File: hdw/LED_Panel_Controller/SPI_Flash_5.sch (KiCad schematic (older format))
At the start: 14 parts, among them U2901 74LVC1G97, U2902 SST25VF080B-50-4I-S2AF

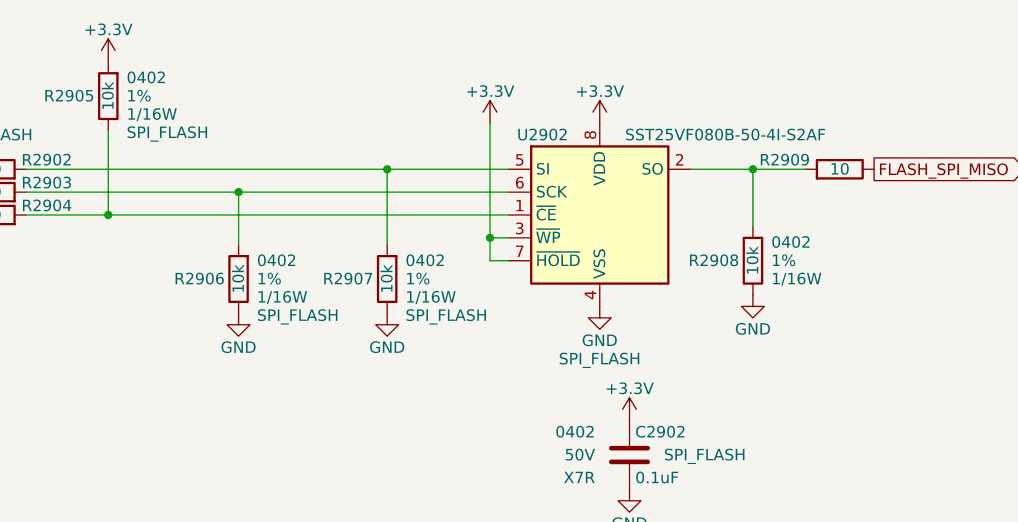
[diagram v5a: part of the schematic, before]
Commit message: fixed SPI flash pull resistors, more PCB placement
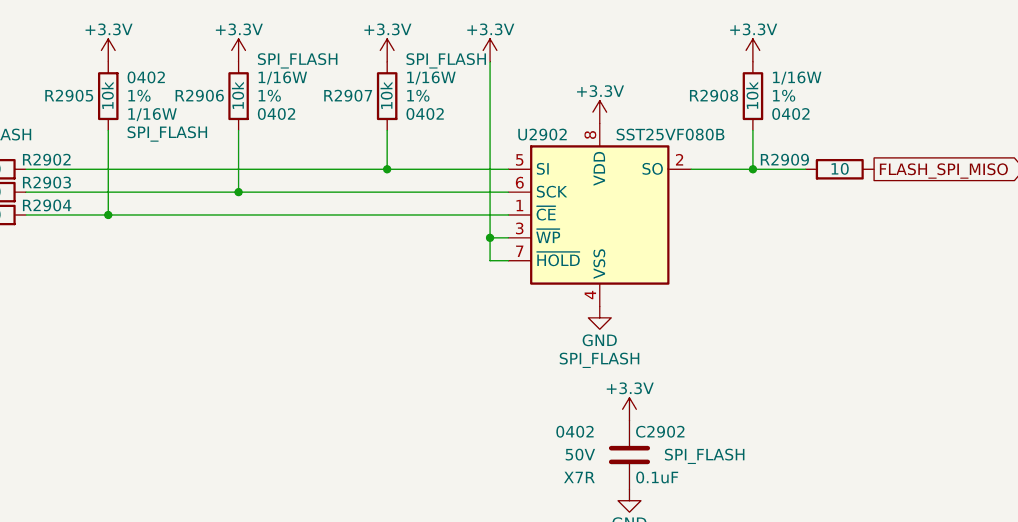
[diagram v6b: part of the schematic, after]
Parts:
- U2902: value SST25VF080B-50-4I-S2AF -> SST25VF080B
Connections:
- net +3V3: now also R2906.2, R2907.2, R2908.2
- net GND: no longer R2906.2, R2907.2, R2908.2
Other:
- moved on the sheet: R2906, R2907, R2908
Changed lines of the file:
@@
 L Custom_Library:R_Custom R2908
 U 1 1 60786266
-P 6750 3850
-F 0 "R2908" H 6690 3850 50  0000 R CNN
-F 1 "10k" V 6750 3850 50  0000 C CNN
-F 2 "Resistors_SMD:R_0402" H 6750 3850 50  0001 C CNN
-F 3 "" H 6750 3850 50  0001 C CNN
-F 4 "0402" H 6830 3930 50  0000 L CNN "display_footprint"
-F 5 "1%" H 6830 3850 50  0000 L CNN "Tolerance"
-F 6 "1/16W" H 6830 3770 50  0000 L CNN "Wattage"
-F 7 "RMCF0402FT10K0CT-ND" H 7050 4250 60  0001 C CNN "Digi-Key PN"
-	1    6750 3850
-	1    0    0    -1
-$EndComp
-$Comp
-L power:GND #PWR02908
-U 1 1 60786271
-P 5150 4080
-F 0 "#PWR02908" H 5150 3830 50  0001 C CNN
-F 1 "GND" H 5150 3930 50  0000 C CNN
-F 2 "" H 5150 4080 50  0001 C CNN
-F 3 "" H 5150 4080 50  0001 C CNN
-	1    5150 4080
-	1    0    0    -1
-$EndComp
-$Comp
-L power:GND #PWR02914
-U 1 1 60786276
-P 6750 4000
-F 0 "#PWR02914" H 6750 3750 50  0001 C CNN
-F 1 "GND" H 6750 3850 50  0000 C CNN
-F 2 "" H 6750 4000 50  0001 C CNN
-F 3 "" H 6750 4000 50  0001 C CNN
-	1    6750 4000
-	1    0    0    -1
+P 6750 3130
+F 0 "R2908" H 6690 3130 50  0000 R CNN
+F 1 "10k" V 6750 3130 50  0000 C CNN
+F 2 "Resistors_SMD:R_0402" H 6750 3130 50  0001 C CNN
+F 3 "" H 6750 3130 50  0001 C CNN
+F 4 "0402" H 6830 3210 50  0000 L CNN "display_footprint"
+F 5 "1%" H 6830 3130 50  0000 L CNN "Tolerance"
+F 6 "1/16W" H 6830 3050 50  0000 L CNN "Wattage"
+F 7 "RMCF0402FT10K0CT-ND" H 7050 3530 60  0001 C CNN "Digi-Key PN"
+	1    6750 3130
+	1    0    0    1
 $EndComp
 $Comp
@@
 $EndComp
 Wire Wire Line
-	5150 3450 5150 3780
-Connection ~ 5150 3450
-Wire Wire Line
-	5150 3450 5680 3450
-Wire Wire Line
 	3930 3280 3930 3650
 Wire Wire Line
 	3930 3650 5680 3650
 Connection ~ 3930 3650
-Wire Wire Line
-	6980 3450 6750 3450
-Wire Wire Line
-	6750 3700 6750 3450
-Connection ~ 6750 3450
-Wire Wire Line
-	6750 3450 6480 3450
 Text GLabel 7280 3450 2    50   Output ~ 0
 FLASH_SPI_MISO
@@
 P 6080 3650
 F 0 "U2902" H 5830 4000 50  0000 C CNN
-F 1 "SST25VF080B-50-4I-S2AF" H 6630 4000 50  0000 C CNN
+F 1 "SST25VF080B" H 6630 4000 50  0000 R CNN
 F 2 "Package_SO:SOIC-8_5.275x5.275mm_P1.27mm" H 6080 2950 50  0001 C CNN
 F 3 "http://ww1.microchip.com/downloads/en/DeviceDoc/20005045C.pdf" H 6030 4200 50  0001 C CNN
@@
 L power:+3.3V #PWR02909
 U 1 1 5F69329F
-P 5600 3250
-F 0 "#PWR02909" H 5600 3100 50  0001 C CNN
-F 1 "+3.3V" H 5600 3390 50  0000 C CNN
-F 2 "" H 5600 3250 50  0001 C CNN
-F 3 "" H 5600 3250 50  0001 C CNN
-	1    5600 3250
+P 5600 2980
+F 0 "#PWR02909" H 5600 2830 50  0001 C CNN
+F 1 "+3.3V" H 5600 3120 50  0000 C CNN
+F 2 "" H 5600 2980 50  0001 C CNN
+F 3 "" H 5600 2980 50  0001 C CNN
+	1    5600 2980
 	1    0    0    -1
 $EndComp
@@
 	5680 3750 5600 3750
 Wire Wire Line
-	5600 3750 5600 3250
+	5600 3750 5600 2980
 Wire Wire Line
 	5680 3850 5600 3850
@@
 	5600 3850 5600 3750
 Connection ~ 5600 3750
-Wire Wire Line
-	3570 3550 4500 3550
 $Comp
 L Custom_Library:R_Custom R2906
 U 1 1 60786316
-P 4500 3930
-F 0 "R2906" H 4440 3930 50  0000 R CNN
-F 1 "10k" V 4500 3930 50  0000 C CNN
-F 2 "Resistors_SMD:R_0402" H 4500 3930 50  0001 C CNN
-F 3 "" H 4500 3930 50  0001 C CNN
-F 4 "0402" H 4580 4010 50  0000 L CNN "display_footprint"
-F 5 "1%" H 4580 3930 50  0000 L CNN "Tolerance"
-F 6 "1/16W" H 4580 3850 50  0000 L CNN "Wattage"
-F 7 "RMCF0402FT10K0CT-ND" H 4800 4330 60  0001 C CNN "Digi-Key PN"
-F 8 "SPI_FLASH" H 4580 3770 50  0000 L CNN "Configuration"
-	1    4500 3930
-	1    0    0    -1
-$EndComp
-$Comp
-L power:GND #PWR02907
-U 1 1 5F697052
-P 4500 4080
-F 0 "#PWR02907" H 4500 3830 50  0001 C CNN
-F 1 "GND" H 4500 3930 50  0000 C CNN
-F 2 "" H 4500 4080 50  0001 C CNN
-F 3 "" H 4500 4080 50  0001 C CNN
-	1    4500 4080
-	1    0    0    -1
-$EndComp
-Wire Wire Line
-	3570 3450 5150 3450
-Wire Wire Line
-	4500 3550 4500 3780
-Connection ~ 4500 3550
-Wire Wire Line
-	4500 3550 5680 3550
+P 4500 3130
+F 0 "R2906" H 4440 3130 50  0000 R CNN
+F 1 "10k" V 4500 3130 50  0000 C CNN
+F 2 "Resistors_SMD:R_0402" H 4500 3130 50  0001 C CNN
+F 3 "" H 4500 3130 50  0001 C CNN
+F 4 "0402" H 4580 3210 50  0000 L CNN "display_footprint"
+F 5 "1%" H 4580 3130 50  0000 L CNN "Tolerance"
+F 6 "1/16W" H 4580 3050 50  0000 L CNN "Wattage"
+F 7 "RMCF0402FT10K0CT-ND" H 4800 3530 60  0001 C CNN "Digi-Key PN"
+F 8 "SPI_FLASH" H 4580 2970 50  0000 L CNN "Configuration"
+	1    4500 3130
+	1    0    0    1
+$EndComp
 $Comp
 L Custom_Library:R_Custom R2903
@@
 L Custom_Library:R_Custom R2907
 U 1 1 60786356
-P 5150 3930
-F 0 "R2907" H 5090 3930 50  0000 R CNN
-F 1 "10k" V 5150 3930 50  0000 C CNN
-F 2 "Resistors_SMD:R_0402" H 5150 3930 50  0001 C CNN
-F 3 "" H 5150 3930 50  0001 C CNN
-F 4 "0402" H 5230 4010 50  0000 L CNN "display_footprint"
-F 5 "1%" H 5230 3930 50  0000 L CNN "Tolerance"
-F 6 "1/16W" H 5230 3850 50  0000 L CNN "Wattage"
-F 7 "RMCF0402FT10K0CT-ND" H 5450 4330 60  0001 C CNN "Digi-Key PN"
-F 8 "SPI_FLASH" H 5230 3770 50  0000 L CNN "Configuration"
-	1    5150 3930
-	1    0    0    -1
+P 5150 3130
+F 0 "R2907" H 5090 3130 50  0000 R CNN
+F 1 "10k" V 5150 3130 50  0000 C CNN
+F 2 "Resistors_SMD:R_0402" H 5150 3130 50  0001 C CNN
+F 3 "" H 5150 3130 50  0001 C CNN
+F 4 "0402" H 5230 3210 50  0000 L CNN "display_footprint"
+F 5 "1%" H 5230 3130 50  0000 L CNN "Tolerance"
+F 6 "1/16W" H 5230 3050 50  0000 L CNN "Wattage"
+F 7 "RMCF0402FT10K0CT-ND" H 5450 3530 60  0001 C CNN "Digi-Key PN"
+F 8 "SPI_FLASH" H 5230 2970 50  0000 L CNN "Configuration"
+	1    5150 3130
+	1    0    0    1
 $EndComp
 $Comp
@@
 	1    0    0    -1
 $EndComp
+Wire Wire Line
+	3570 3450 5150 3450
+Wire Wire Line
+	3570 3550 4500 3550
+$Comp
+L power:+3.3V #PWR0118
+U 1 1 6069578E
+P 5150 2980
+F 0 "#PWR0118" H 5150 2830 50  0001 C CNN
+F 1 "+3.3V" H 5150 3120 50  0000 C CNN
+F 2 "" H 5150 2980 50  0001 C CNN
+F 3 "" H 5150 2980 50  0001 C CNN
+	1    5150 2980
+	1    0    0    -1
+$EndComp
+$Comp
+L power:+3.3V #PWR0119
+U 1 1 60695CEE
+P 4500 2980
+F 0 "#PWR0119" H 4500 2830 50  0001 C CNN
+F 1 "+3.3V" H 4500 3120 50  0000 C CNN
+F 2 "" H 4500 2980 50  0001 C CNN
+F 3 "" H 4500 2980 50  0001 C CNN
+	1    4500 2980
+	1    0    0    -1
+$EndComp
+Wire Wire Line
+	4500 3280 4500 3550
+Connection ~ 4500 3550
+Wire Wire Line
+	4500 3550 5680 3550
+Wire Wire Line
+	5150 3280 5150 3450
+Connection ~ 5150 3450
+Wire Wire Line
+	5150 3450 5680 3450
+Wire Wire Line
+	6480 3450 6750 3450
+$Comp
+L power:+3.3V #PWR0120
+U 1 1 60696E84
+P 6750 2980
+F 0 "#PWR0120" H 6750 2830 50  0001 C CNN
+F 1 "+3.3V" H 6750 3120 50  0000 C CNN
+F 2 "" H 6750 2980 50  0001 C CNN
+F 3 "" H 6750 2980 50  0001 C CNN
+	1    6750 2980
+	1    0    0    -1
+$EndComp
+Wire Wire Line
+	6750 3280 6750 3450
+Connection ~ 6750 3450
+Wire Wire Line
+	6750 3450 6980 3450
 $EndSCHEMATC

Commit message: added BOMs, some consolidation
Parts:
- C2901, C2902: Digi-Key PN 490-10701-1-ND -> 490-10698-1-ND
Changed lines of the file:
@@
 F 5 "50V" H 1860 6900 50  0000 R CNN "Voltage"
 F 6 "X7R" H 1860 6800 50  0000 R CNN "Dielectric"
-F 7 "490-10701-1-ND" H 2435 7400 60  0001 C CNN "Digi-Key PN"
+F 7 "490-10698-1-ND" H 2435 7400 60  0001 C CNN "Digi-Key PN"
 F 8 "SPI_FLASH" H 2340 6900 50  0000 C CNN "Configuration"
 	1    2010 6900
@@
 F 5 "50V" H 6060 4700 50  0000 R CNN "Voltage"
 F 6 "X7R" H 6060 4600 50  0000 R CNN "Dielectric"
-F 7 "490-10701-1-ND" H 6635 5200 60  0001 C CNN "Digi-Key PN"
+F 7 "490-10698-1-ND" H 6635 5200 60  0001 C CNN "Digi-Key PN"
 F 8 "SPI_FLASH" H 6540 4700 50  0000 C CNN "Configuration"
 	1    6210 4700
